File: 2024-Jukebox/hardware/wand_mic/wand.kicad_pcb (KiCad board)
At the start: 4 copper layers, 40.7 x 32 mm, 51 parts, among them J1 USB_C_Receptacle_USB2.0, J2 Conn_01x05, J3 Conn_01x07, J5 Conn_01x04, J6 Conn_01x01, J7 Conn_01x04, J8 Conn_01x07, Q1 MUN5214DW1T1G, Q2 BSS138, Q3 CJ3139K, Q5 BSS138, SW1 SW_SPDT, U1 CP2104, U2 ESP32-PICO-D4, U3 ICM-20948, U4 TP4065-4.2V, U5 NCP167BMX330TBG, U6 LY68L6400SLIT, U7 MIC5225-1.8

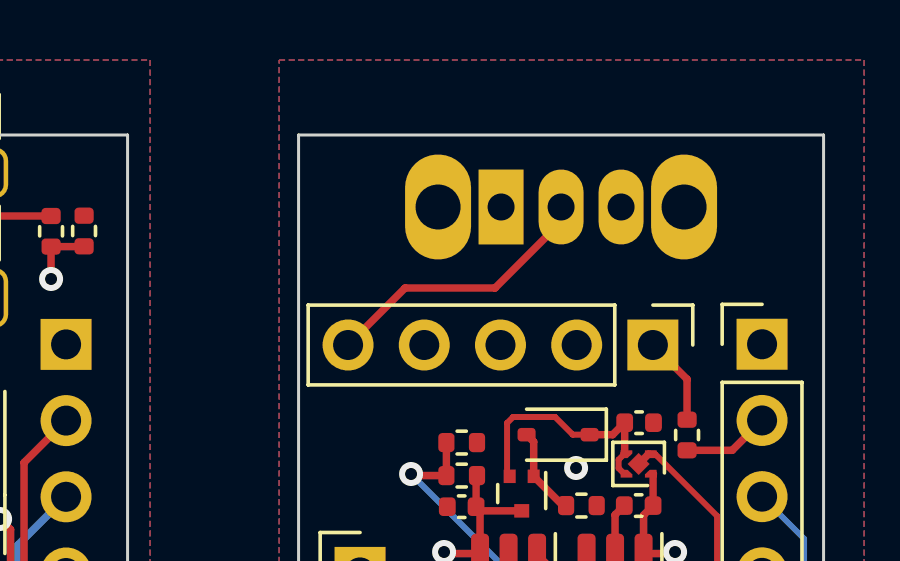
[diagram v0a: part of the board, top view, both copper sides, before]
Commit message: Added power selection jumper for LED
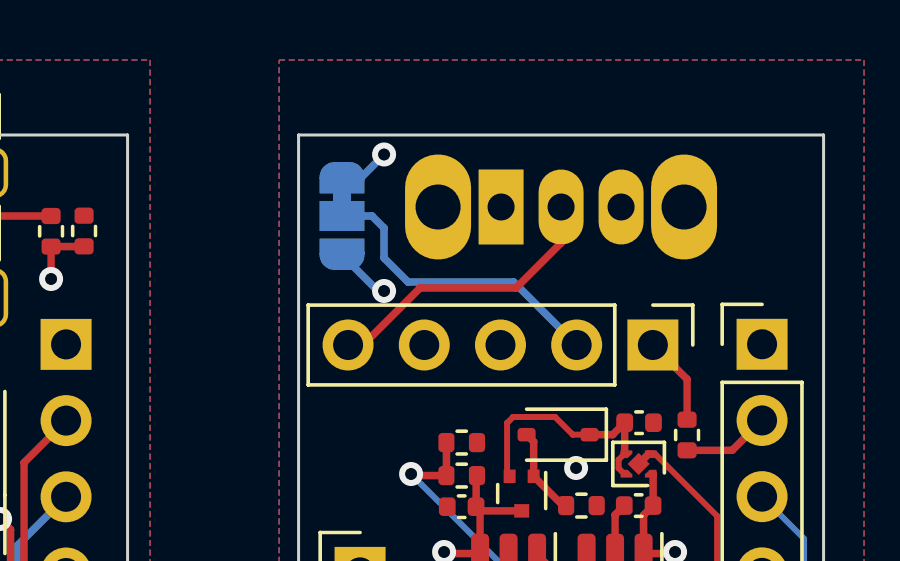
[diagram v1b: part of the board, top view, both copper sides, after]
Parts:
- added JP1: SolderJumper_3_Bridged12, Jumper:SolderJumper-3_P1.3mm_Bridged12_RoundedPad1.0x1.5mm, B.Cu at (23.9, 2.70)
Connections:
- J2 pad 2: +BATT -> Net-(J2-Pin_2)
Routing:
- net Net-(J2-Pin_2): track 0.00 -> 10.2 mm
- net +BATT: track 5.47 -> 7.36 mm, vias 1 -> 2
- net +3V3: track 36.2 -> 37.9 mm, vias 8 -> 9
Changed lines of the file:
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@@
   (net 95 "Net-(J2-Pin_1)")
   (net 96 "Net-(J6-Pin_1)")
+  (net 97 "Net-(J2-Pin_2)")
   (footprint "Capacitor_SMD:C_1206_3216Metric" (layer "F.Cu")
     (at 5.4 30.3 180)
@@
       (net 95 "Net-(J2-Pin_1)") (pinfunction "Pin_1") (pintype "passive"))
     (pad "2" thru_hole oval (at 0 2.54 270) (size 1.7 1.7) (drill 1) (layers "*.Cu" "*.Mask")
-      (net 66 "+BATT") (pinfunction "Pin_2") (pintype "passive"))
+      (net 97 "Net-(J2-Pin_2)") (pinfunction "Pin_2") (pintype "passive"))
     (pad "3" thru_hole oval (at 0 5.08 270) (size 1.7 1.7) (drill 1) (layers "*.Cu" "*.Mask")
       (net 6 "GND") (pinfunction "Pin_3") (pintype "passive"))
@@
     )
   )
+  (footprint "Jumper:SolderJumper-3_P1.3mm_Bridged12_RoundedPad1.0x1.5mm" (layer "B.Cu")
+    (at 23.9 2.7 -90)
+    (descr "SMD Solder 3-pad Jumper, 1x1.5mm rounded Pads, 0.3mm gap, pads 1-2 bridged with 1 copper strip")
+    (tags "net tie solder jumper bridged")
+    (property "Sheetfile" "wand.kicad_sch")
+    (property "Sheetname" "")
+    (property "ki_description" "3-pole Solder Jumper, pins 1+2 closed/bridged")
+    (property "ki_keywords" "Solder Jumper SPDT")
+    (attr exclude_from_pos_files)
+    (net_tie_pad_groups "1, 2, 3")
+    (fp_text reference "JP1" (at 0 1.8 90) (layer "B.SilkS") hide
+        (effects (font (size 1 1) (thickness 0.15)) (justify mirror))
+    )
+    (fp_text value "SolderJumper_3_Bridged12" (at 0 -1.9 90) (layer "B.Fab")
+        (effects (font (size 1 1) (thickness 0.15)) (justify mirror))
+    )
+    (fp_poly
+      (pts
+        (xy -0.9 0.3)
+        (xy -0.4 0.3)
+        (xy -0.4 -0.3)
+        (xy -0.9 -0.3)
+      )
+      (stroke (width 0) (type solid)) (fill solid) (layer "B.Cu"))
+    (fp_line (start -2.05 -0.3) (end -2.05 0.3)
+      (stroke (width 0.12) (type solid)) (layer "B.SilkS"))
+    (fp_line (start -1.5 -1.5) (end -0.9 -1.5)
+      (stroke (width 0.12) (type solid)) (layer "B.SilkS"))
+    (fp_line (start -1.4 1) (end 1.4 1)
+      (stroke (width 0.12) (type solid)) (layer "B.SilkS"))
+    (fp_line (start -1.2 -1.2) (end -1.5 -1.5)
+      (stroke (width 0.12) (type solid)) (layer "B.SilkS"))
+    (fp_line (start -1.2 -1.2) (end -0.9 -1.5)
+      (stroke (width 0.12) (type solid)) (layer "B.SilkS"))
+    (fp_line (start 1.4 -1) (end -1.4 -1)
+      (stroke (width 0.12) (type solid)) (layer "B.SilkS"))
+    (fp_line (start 2.05 0.3) (end 2.05 -0.3)
+      (stroke (width 0.12) (type solid)) (layer "B.SilkS"))
+    (fp_arc (start -2.05 -0.3) (mid -1.844975 -0.794975) (end -1.35 -1)
+      (stroke (width 0.12) (type solid)) (layer "B.SilkS"))
+    (fp_arc (start -1.35 1) (mid -1.844975 0.794975) (end -2.05 0.3)
+      (stroke (width 0.12) (type solid)) (layer "B.SilkS"))
+    (fp_arc (start 1.35 -1) (mid 1.844975 -0.794975) (end 2.05 -0.3)
+      (stroke (width 0.12) (type solid)) (layer "B.SilkS"))
+    (fp_arc (start 2.05 0.3) (mid 1.844975 0.794975) (end 1.35 1)
+      (stroke (width 0.12) (type solid)) (layer "B.SilkS"))
+    (fp_line (start -2.3 1.25) (end -2.3 -1.25)
+      (stroke (width 0.05) (type solid)) (layer "B.CrtYd"))
+    (fp_line (start -2.3 1.25) (end 2.3 1.25)
+      (stroke (width 0.05) (type solid)) (layer "B.CrtYd"))
+    (fp_line (start 2.3 -1.25) (end -2.3 -1.25)
+      (stroke (width 0.05) (type solid)) (layer "B.CrtYd"))
+    (fp_line (start 2.3 -1.25) (end 2.3 1.25)
+      (stroke (width 0.05) (type solid)) (layer "B.CrtYd"))
+    (pad "1" smd custom (at -1.3 0 270) (size 1 0.5) (layers "B.Cu" "B.Mask")
+      (net 70 "+3V3") (pinfunction "A") (pintype "passive") (zone_connect 2)
+      (options (clearance outline) (anchor rect))
+      (primitives
+        (gr_circle (center 0 -0.25) (end 0.5 -0.25) (width 0) (fill yes))
+        (gr_circle (center 0 0.25) (end 0.5 0.25) (width 0) (fill yes))
+        (gr_poly
+          (pts
+            (xy 0.55 -0.75)
+            (xy 0 -0.75)
+            (xy 0 0.75)
+            (xy 0.55 0.75)
+          )
+          (width 0) (fill yes))
+      ))
+    (pad "2" smd rect (at 0 0 270) (size 1 1.5) (layers "B.Cu" "B.Mask")
+      (net 97 "Net-(J2-Pin_2)") (pinfunction "C") (pintype "passive"))
+    (pad "3" smd custom (at 1.3 0 270) (size 1 0.5) (layers "B.Cu" "B.Mask")
+      (net 66 "+BATT") (pinfunction "B") (pintype "passive") (zone_connect 2)
+      (options (clearance outline) (anchor rect))
+      (primitives
+        (gr_circle (center 0 -0.25) (end 0.5 -0.25) (width 0) (fill yes))
+        (gr_circle (center 0 0.25) (end 0.5 0.25) (width 0) (fill yes))
+        (gr_poly
+          (pts
+            (xy 0 -0.75)
+            (xy -0.55 -0.75)
+            (xy -0.55 0.75)
+            (xy 0 0.75)
+          )
+          (width 0) (fill yes))
+      ))
+  )
   (footprint "Button_Switch_THT:SW_CuK_OS102011MA1QN1_SPDT_Angled" (layer "B.Cu")
     (at 29.2 2.4)
@@
   (segment (start 28.505 12.5275) (end 28.3675 12.39) (width 0.25) (layer "F.Cu") (net 66))
   (via (at 27.3 13.9) (size 0.8) (drill 0.4) (layers "F.Cu" "B.Cu") (net 66))
+  (via (at 25.3 5.2) (size 0.8) (drill 0.4) (layers "F.Cu" "B.Cu") (net 66))
+  (segment (start 25.3 5.2) (end 25.1 5.2) (width 0.25) (layer "B.Cu") (net 66))
+  (segment (start 25.1 5.2) (end 23.9 4) (width 0.25) (layer "B.Cu") (net 66))
   (segment (start 10.25 26.974598) (end 10.25 26.45) (width 0.25) (layer "F.Cu") (net 67))
   (segment (start 27.3775 11.3525) (end 27.3775 10.2525) (width 0.25) (layer "F.Cu") (net 67))
@@
   (via (at 3 23.8) (size 0.8) (drill 0.4) (layers "F.Cu" "B.Cu") (net 70))
   (via (at 30.6 20.1) (size 0.8) (drill 0.4) (layers "F.Cu" "B.Cu") (net 70))
+  (via (at 25.3 0.6495) (size 0.8) (drill 0.4) (layers "F.Cu" "B.Cu") (net 70))
   (via (at 7 27.6) (size 0.8) (drill 0.4) (layers "F.Cu" "B.Cu") (net 70))
   (segment (start 33.2 25.1) (end 33.2 23.9) (width 0.25) (layer "In1.Cu") (net 70))
   (segment (start 6.8 27.4) (end 6.8 26.5) (width 0.25) (layer "In1.Cu") (net 70))
   (segment (start 7 27.6) (end 6.8 27.4) (width 0.25) (layer "In1.Cu") (net 70))
+  (segment (start 24.5495 1.4) (end 23.9 1.4) (width 0.25) (layer "B.Cu") (net 70))
+  (segment (start 25.3 0.6495) (end 24.5495 1.4) (width 0.25) (layer "B.Cu") (net 70))
   (segment (start 2 7.9) (end 2.5 7.9) (width 0.25) (layer "F.Cu") (net 71))
   (segment (start 3.028893 22.33955) (end 3.118443 22.25) (width 0.25) (layer "F.Cu") (net 72))
@@
   (segment (start 34 24) (end 32.4 24) (width 0.2) (layer "F.Cu") (net 91))
   (segment (start 32.07 22.23) (end 32.07 23.2525) (width 0.25) (layer "F.Cu") (net 91))
-  (segment (start 31.2 2.4) (end 31.2 2.9) (width 0.25) (layer "F.Cu") (net 94))
-  (segment (start 31.2 2.9) (end 29 5.1) (width 0.25) (layer "F.Cu") (net 94))
-  (segment (start 26 5.1) (end 24.1 7) (width 0.25) (layer "F.Cu") (net 94))
-  (segment (start 29 5.1) (end 26 5.1) (width 0.25) (layer "F.Cu") (net 94))
+  (segment (start 24.6 7) (end 26.5 5.1) (width 0.25) (layer "F.Cu") (net 94))
+  (segment (start 24.1 7) (end 24.6 7) (width 0.25) (layer "F.Cu") (net 94))
+  (segment (start 29.7 5.1) (end 31.2 3.6) (width 0.25) (layer "F.Cu") (net 94))
+  (segment (start 31.2 3.6) (end 31.2 2.4) (width 0.25) (layer "F.Cu") (net 94))
+  (segment (start 26.5 5.1) (end 29.7 5.1) (width 0.25) (layer "F.Cu") (net 94))
   (segment (start 35.4 8.14) (end 34.26 7) (width 0.25) (layer "F.Cu") (net 95))
   (segment (start 35.4 9.49) (end 35.4 8.14) (width 0.25) (layer "F.Cu") (net 95))
   (segment (start 12.3 28) (end 12.3 30) (width 0.25) (layer "F.Cu") (net 96))
   (segment (start 10.75 26.45) (end 12.3 28) (width 0.25) (layer "F.Cu") (net 96))
+  (segment (start 26.1 4.9) (end 29.62 4.9) (width 0.25) (layer "B.Cu") (net 97))
+  (segment (start 29.62 4.9) (end 31.72 7) (width 0.25) (layer "B.Cu") (net 97))
+  (segment (start 25.3 4.1) (end 26.1 4.9) (width 0.25) (layer "B.Cu") (net 97))
+  (segment (start 24.9 2.7) (end 25.3 3.1) (width 0.25) (layer "B.Cu") (net 97))
+  (segment (start 25.3 3.1) (end 25.3 4.1) (width 0.25) (layer "B.Cu") (net 97))
+  (segment (start 23.9 2.7) (end 24.9 2.7) (width 0.25) (layer "B.Cu") (net 97))
   (zone (net 6) (net_name "GND") (layers "F&B.Cu") (hatch edge 0.5)
     (connect_pads (clearance 0.508))
